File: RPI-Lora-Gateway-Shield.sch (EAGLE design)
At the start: 56 parts, among them J1 GROVE, J10 CON_TERMINAL_BLOCK_02-5MM, J11 JUMPER_1X30805, J12 JUMPER_1X30805, J13 GROVE I2C, J14 2.54_I2C, J15 POWER_JACKPTH, J16 2.54_PWR, J4 RASPBERRYPI-40-PIN-GPIO, J5 DHTxx, J6 2.54_I2C, J7 2.54_I2C, J8 CON_TERMINAL_BLOCK_02-5MM, J9 CON_TERMINAL_BLOCK_02-5MM

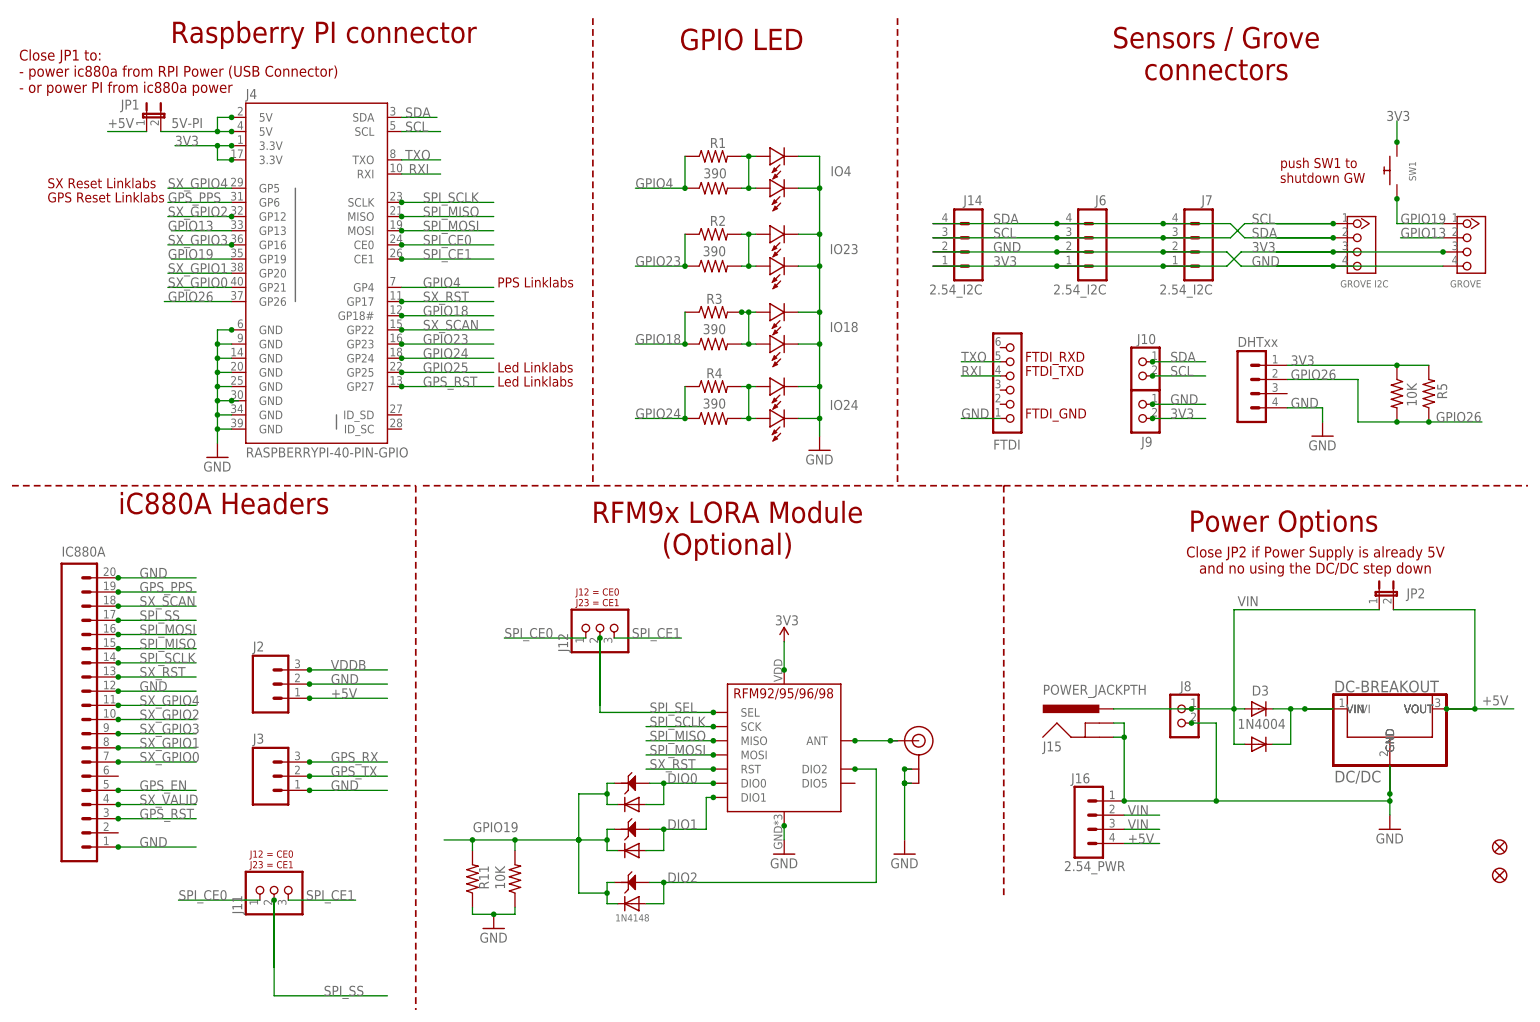
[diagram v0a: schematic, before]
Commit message: removed RFM9x, added GPS Module + INA219 current sensor
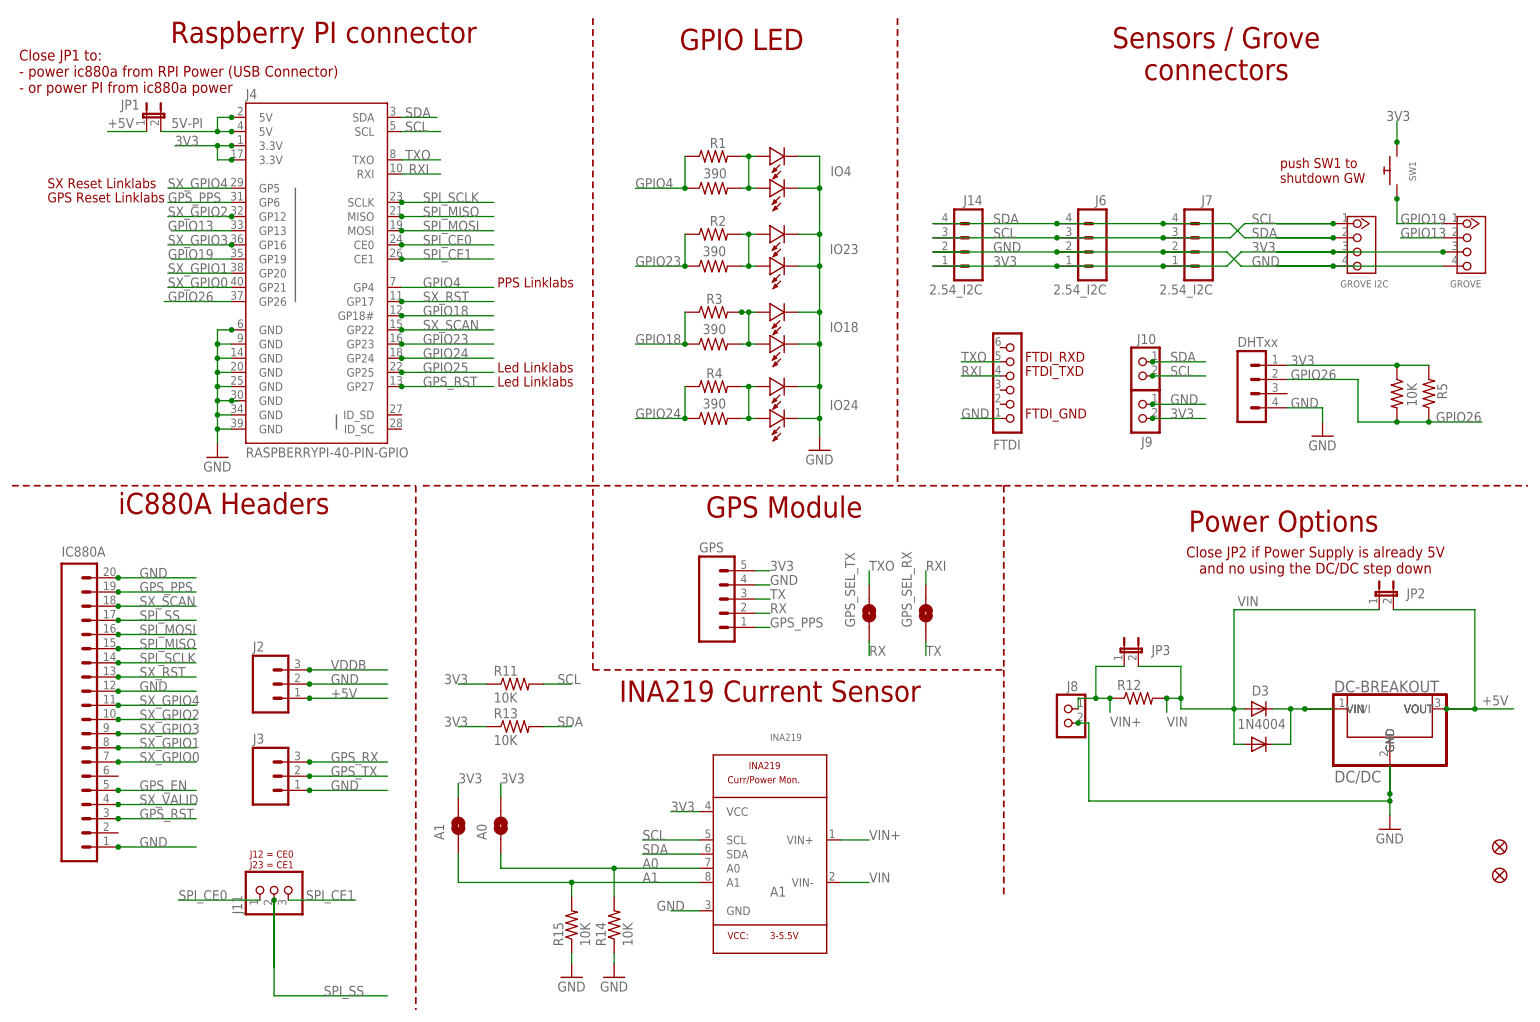
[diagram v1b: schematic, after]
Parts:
- removed D0, D1, D2: 1N4148, Seeed-Discrete:D-ESD-2P-CESD5V0D1
- removed D5: 1N4148, adafruit:DIODEDO-1N4148
- removed D6, D7: (no value), adafruit:DIODEDO-1N4148
- removed J12: JUMPER_1X30805, dp_devices:JUMPER_1X30805
- removed J15: POWER_JACKPTH, SparkFun-Connectors:POWER_JACKPTH
- removed J16: 2.54_PWR, _c2h:CON_HEADER_1X04'NO_LOCK'
- removed U$2: RFM95, _c2h:RFM95
- removed U$3: ANTENNA-UFL, _c2h:ANTENNA-UFL
- added A0, A1, GPS_SEL_RX, GPS_SEL_TX: SOLDERJUMPERNO, SparkFun-Retired:SOLDERJUMPERNO
- added GPS: (no value), SparkFun-Connectors:M05PTH
- added INA219: (no value), INA219:INA219
- added JP3: (no value), microbuilder:JUMPER2
- added R13, R14, R15: 10K, SparkFun-Passives:RESISTOR0805-RES
- R11: device _c2h:RESISTORPTH-1/4W -> SparkFun-Passives:RESISTOR0805-RES
- R12: device _c2h:RESISTOR0805-RES -> adafruit:R-US_R2512
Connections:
- removed net DIO0: D0.1, D6.A, U$2.DIO0
- removed net DIO1: D1.1, D7.A, U$2.DIO1
- removed net DIO2: D2.1, D5.A, U$2.DIO2
- removed net N$29: U$2.ANT, U$3.SIGNAL
- removed net SPI_SEL: J12.2, U$2.SEL
- new net A0: A0.1, INA219.A0, R14.2
- new net A1: A1.1, INA219.A1, R15.2
- new net RX: GPS.2, GPS_SEL_TX.1
- new net TX: GPS.3, GPS_SEL_RX.1
- new net VIN+: INA219.VIN+, J8.1, JP3.1, R12.1
- net +5V: no longer J16.4
- net 3V3: now also A0.2, A1.2, GPS.5, INA219.VCC, R11.1, R13.1; no longer U$2.VCC
- net GND: now also GPS.4, INA219.GND, R14.1, R15.1; no longer J15.GND, J15.GNDBREAK, J16.1, R11.1, R12.1, U$2.GND, U$3.GND@0, U$3.GND@1
- net GPIO19: no longer D0.2, D1.2, D2.2, D5.C, D6.C, D7.C, R11.2, R12.2
- net GPS_PPS: now also GPS.1
- net RXI: now also GPS_SEL_RX.2
- net SCL: now also INA219.SCL, R11.2
- net SDA: now also INA219.SDA, R13.2
- net SPI_CE0: no longer J12.1
- net SPI_CE1: no longer J12.3
- net SPI_MISO: no longer U$2.MISO
- net SPI_MOSI: no longer U$2.MOSI
- net SPI_SCLK: no longer U$2.SCK
- net SX_RST: no longer U$2.RST
- net TXO: now also GPS_SEL_TX.2
- net VIN: now also INA219.VIN-, JP3.2, R12.2; no longer J15.PWR, J16.2, J16.3, J8.1
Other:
- note added: "GPS Module"
- note added: "INA219 Current Sensor"
- note removed: "RFM9x LORA Module (Optional)"
- moved on the sheet: J8, R11

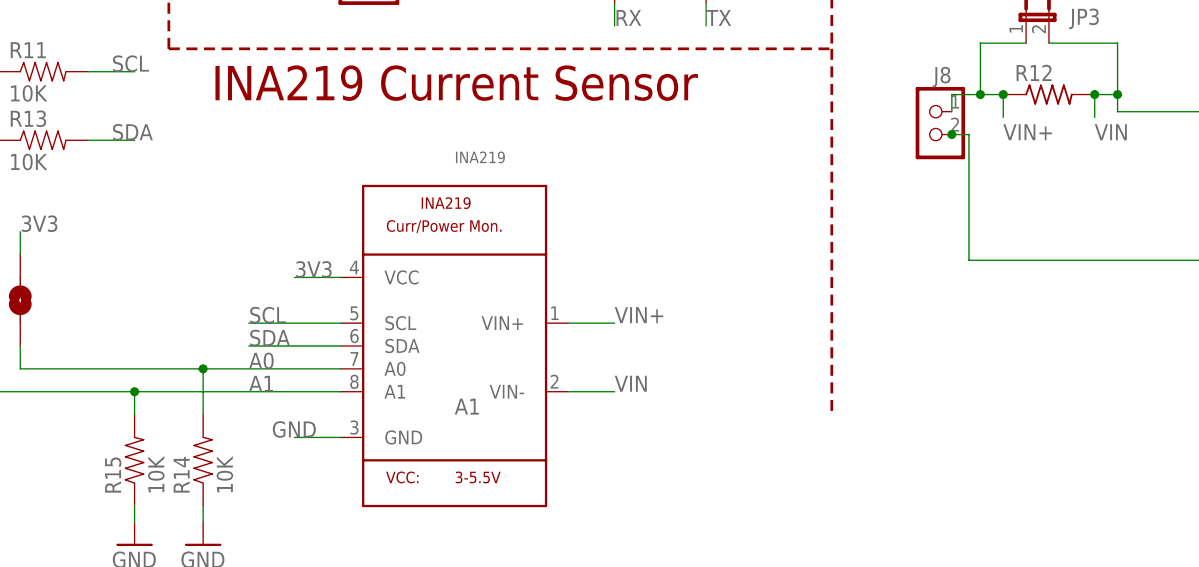
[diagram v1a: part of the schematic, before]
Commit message: added header for volt meter + holes for rasppi zero
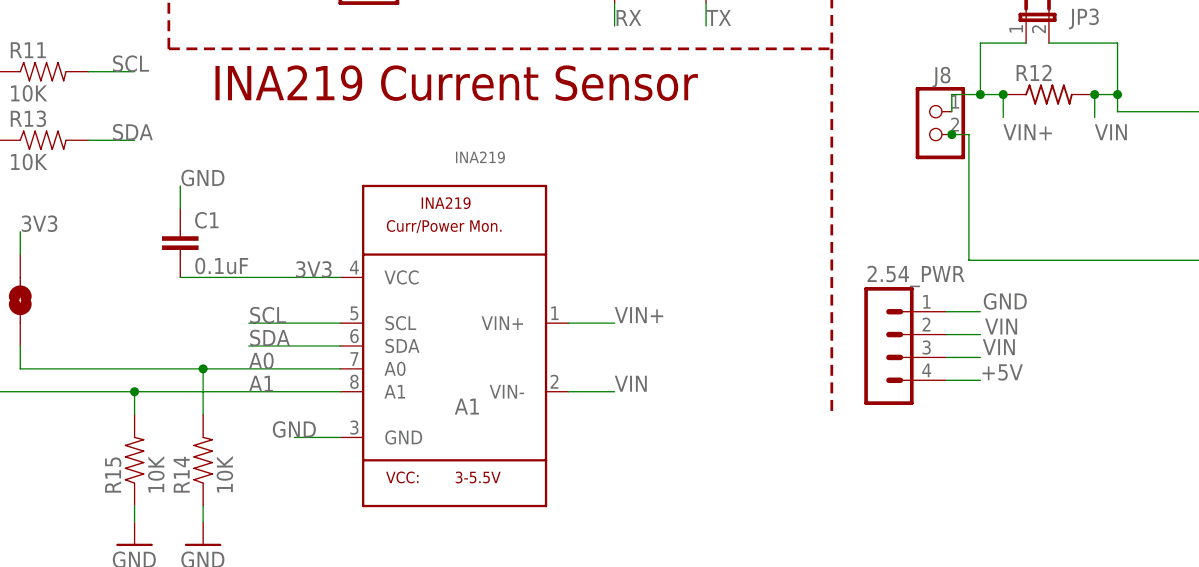
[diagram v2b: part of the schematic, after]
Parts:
- added C1: 0.1uF, SparkFun-Capacitors:2.2UF-25V-+80/-20(0805)
- added J12: 2.54_PWR, _c2h:CON_HEADER_1X04'NO_LOCK'
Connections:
- net +5V: now also J12.4
- net 3V3: now also C1.2
- net GND: now also C1.1, J12.1
- net VIN: now also J12.2, J12.3
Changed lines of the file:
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@@
 <part name="GPS_SEL_TX" library="SparkFun-Retired" deviceset="SOLDERJUMPER" device="NO"/>
 <part name="GPS_SEL_RX" library="SparkFun-Retired" deviceset="SOLDERJUMPER" device="NO"/>
+<part name="J12" library="_c2h" deviceset="CON_HEADER_1X04" device="'NO_LOCK'" value="2.54_PWR"/>
+<part name="C1" library="SparkFun-Capacitors" deviceset="2.2UF-25V-+80/-20(0805)" device="" value="0.1uF"/>
 </parts>
 <sheets>
@@
 <attribute name="NAME" x="129.54" y="-33.02" size="1.778" layer="95" rot="R90"/>
 </instance>
+<instance part="J12" gate="G$1" x="148.59" y="-67.31" smashed="yes" rot="MR180">
+<attribute name="VALUE" x="149.86" y="-64.77" size="1.778" layer="96" rot="MR180"/>
+</instance>
+<instance part="C1" gate="G$1" x="73.66" y="-63.5" smashed="yes">
+<attribute name="NAME" x="75.184" y="-60.579" size="1.778" layer="95"/>
+<attribute name="VALUE" x="75.184" y="-65.659" size="1.778" layer="96"/>
+</instance>
 </instances>
 <busses>
@@
 <wire x1="76.2" y1="-93.218" x2="76.2" y2="-91.44" width="0.1524" layer="91"/>
 </segment>
+<segment>
+<pinref part="J12" gate="G$1" pin="1"/>
+<wire x1="158.75" y1="-69.85" x2="162.56" y2="-69.85" width="0.1524" layer="91"/>
+<label x="162.814" y="-69.596" size="1.778" layer="95"/>
+</segment>
+<segment>
+<pinref part="C1" gate="G$1" pin="1"/>
+<wire x1="73.66" y1="-58.42" x2="73.66" y2="-55.88" width="0.1524" layer="91"/>
+<label x="73.66" y="-55.88" size="1.778" layer="95"/>
+</segment>
 </net>
 <net name="GPIO18" class="0">
@@
 <segment>
 <pinref part="INA219" gate="G$1" pin="VCC"/>
-<wire x1="91.44" y1="-66.04" x2="86.36" y2="-66.04" width="0.1524" layer="91"/>
 <label x="86.36" y="-66.04" size="1.778" layer="95"/>
+<pinref part="C1" gate="G$1" pin="2"/>
+<wire x1="91.44" y1="-66.04" x2="73.66" y2="-66.04" width="0.1524" layer="91"/>
 </segment>
 <segment>
@@
 <label x="121.92" y="-78.74" size="1.778" layer="95"/>
 </segment>
+<segment>
+<pinref part="J12" gate="G$1" pin="2"/>
+<wire x1="158.75" y1="-72.39" x2="162.56" y2="-72.39" width="0.1524" layer="91"/>
+<label x="163.068" y="-72.39" size="1.778" layer="95"/>
+</segment>
+<segment>
+<pinref part="J12" gate="G$1" pin="3"/>
+<wire x1="158.75" y1="-74.93" x2="162.56" y2="-74.93" width="0.1524" layer="91"/>
+<label x="162.814" y="-74.676" size="1.778" layer="95"/>
+</segment>
 </net>
 <net name="+5V" class="0">
@@
 <label x="-14.605" y="56.515" size="1.778" layer="95"/>
 </segment>
-</net>
+<segment>
+<pinref part="J12" gate="G$1" pin="4"/>
+<wire x1="158.75" y1="-77.47" x2="162.56" y2="-77.47" width="0.1524" layer="91"/>
+<label x="162.56" y="-77.47" size="1.778" layer="95"/>
+</segment>
+</net>
